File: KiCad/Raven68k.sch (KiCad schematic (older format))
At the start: 19 parts, among them CON1 BARREL_JACK, P1 CONN_01X06, U1 68000D, U2 28C256, U3 SRAM_512Ko, U4 SRAM_512Ko, U5 28C256, U6 XC9572XL-TQ100, Y1 Crystal_GND24

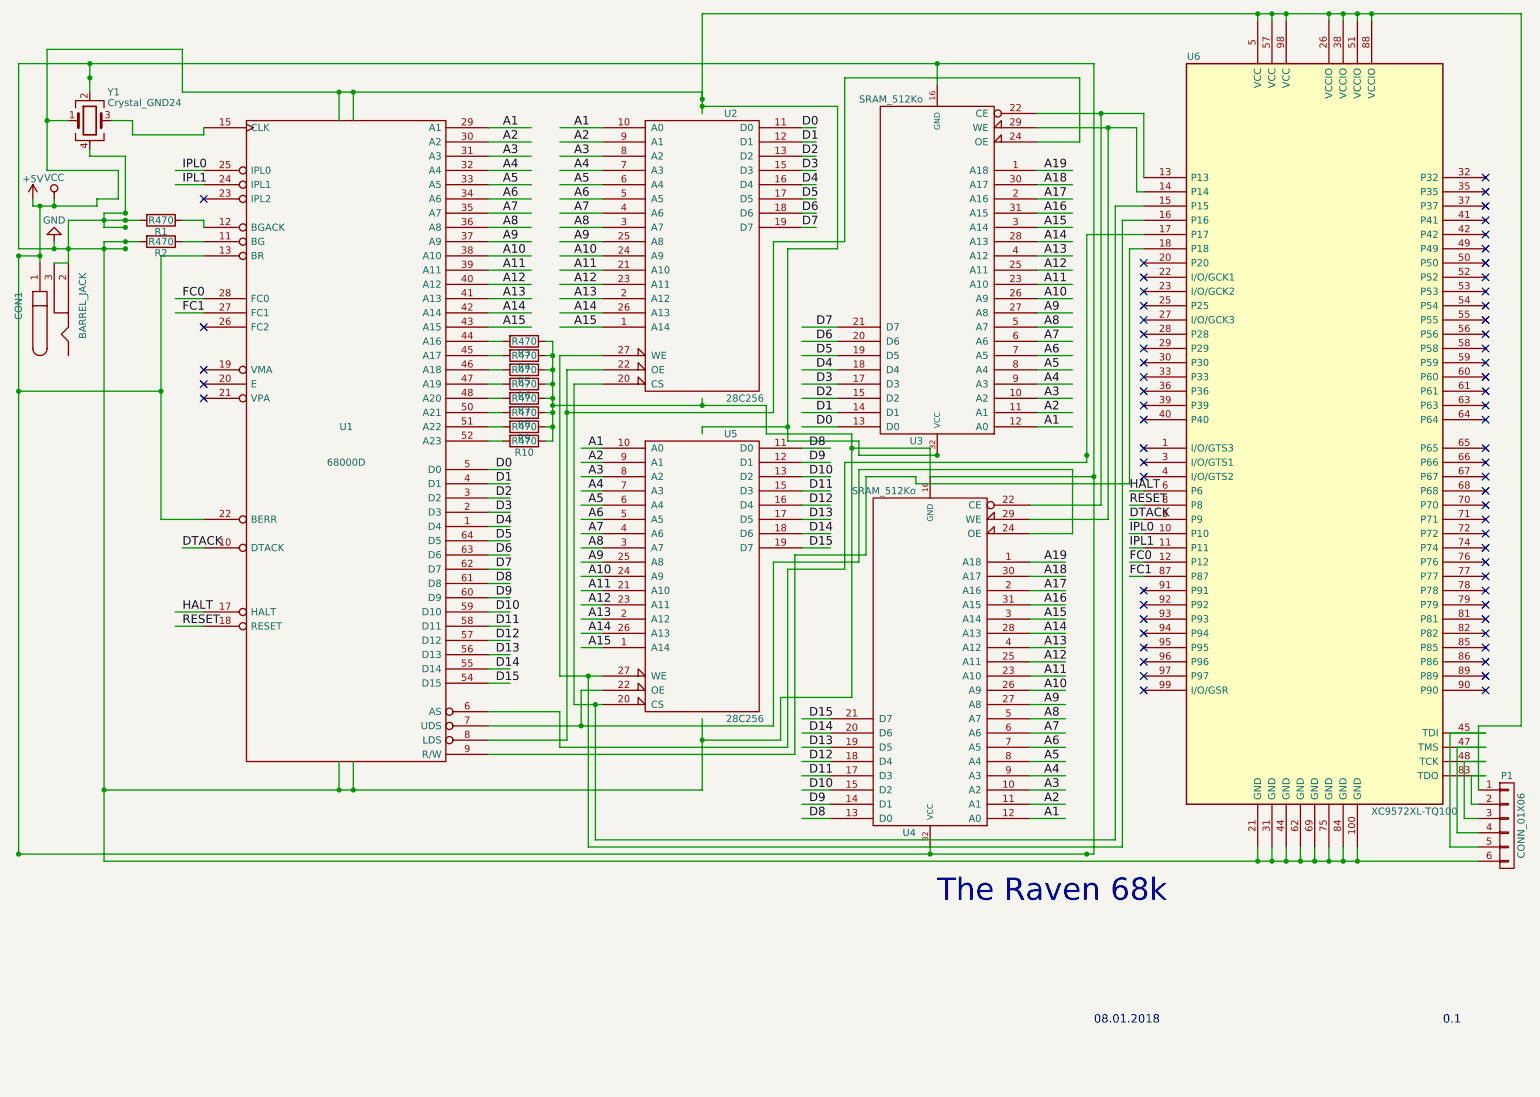
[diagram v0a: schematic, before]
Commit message: Added 68681 DUART.
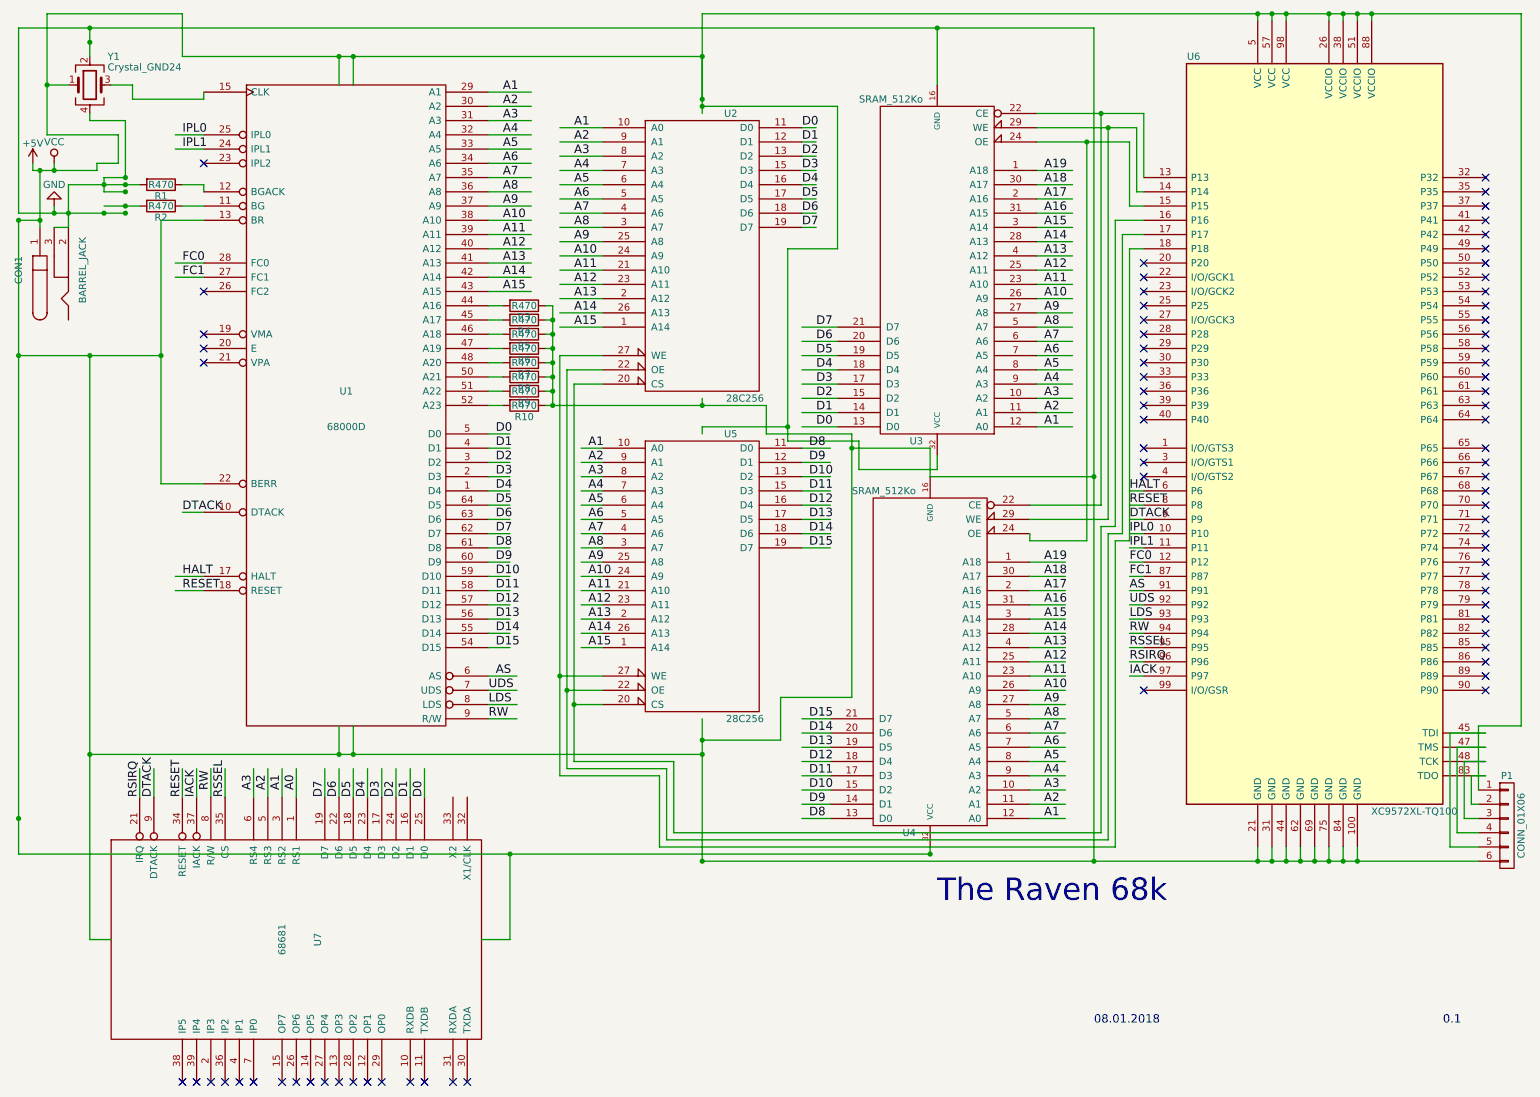
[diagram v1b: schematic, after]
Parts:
- added U7: 68681, symbol 68681
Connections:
- net labels added: A0, AS, IACK, LDS, RSIRQ, RSSEL, RW, UDS
- wire segments 328 -> 345
- no-connect marks 64 -> 75
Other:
- moved on the sheet: CON1, R1, R10, R2, R3, R4, R5, R6, R7, R8, R9, U1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

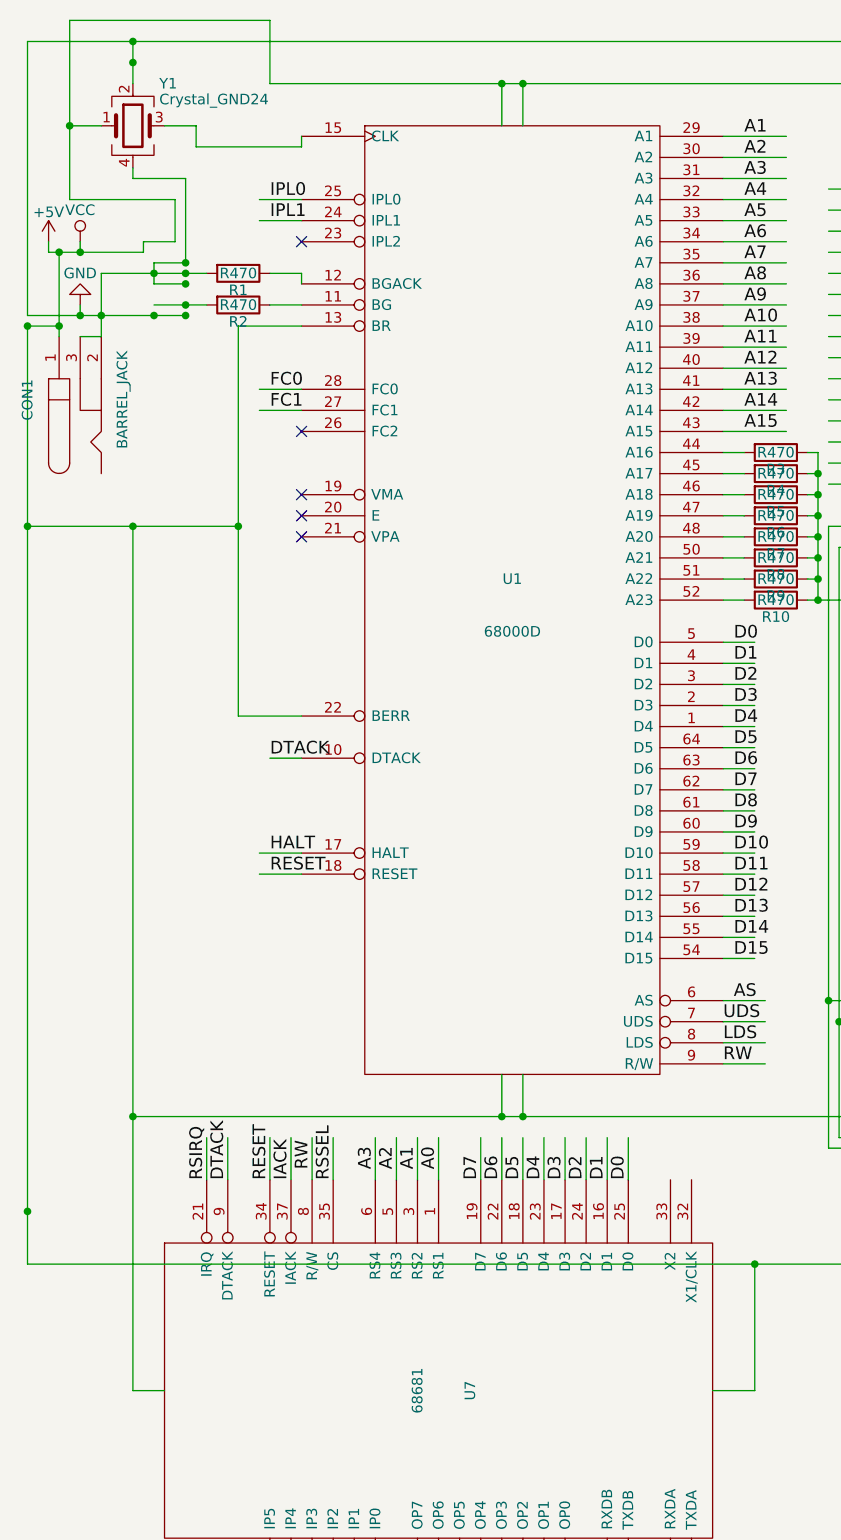
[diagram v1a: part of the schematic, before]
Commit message: Added a few pull-down resistors. Continued schematic re-work started in earlier commit.
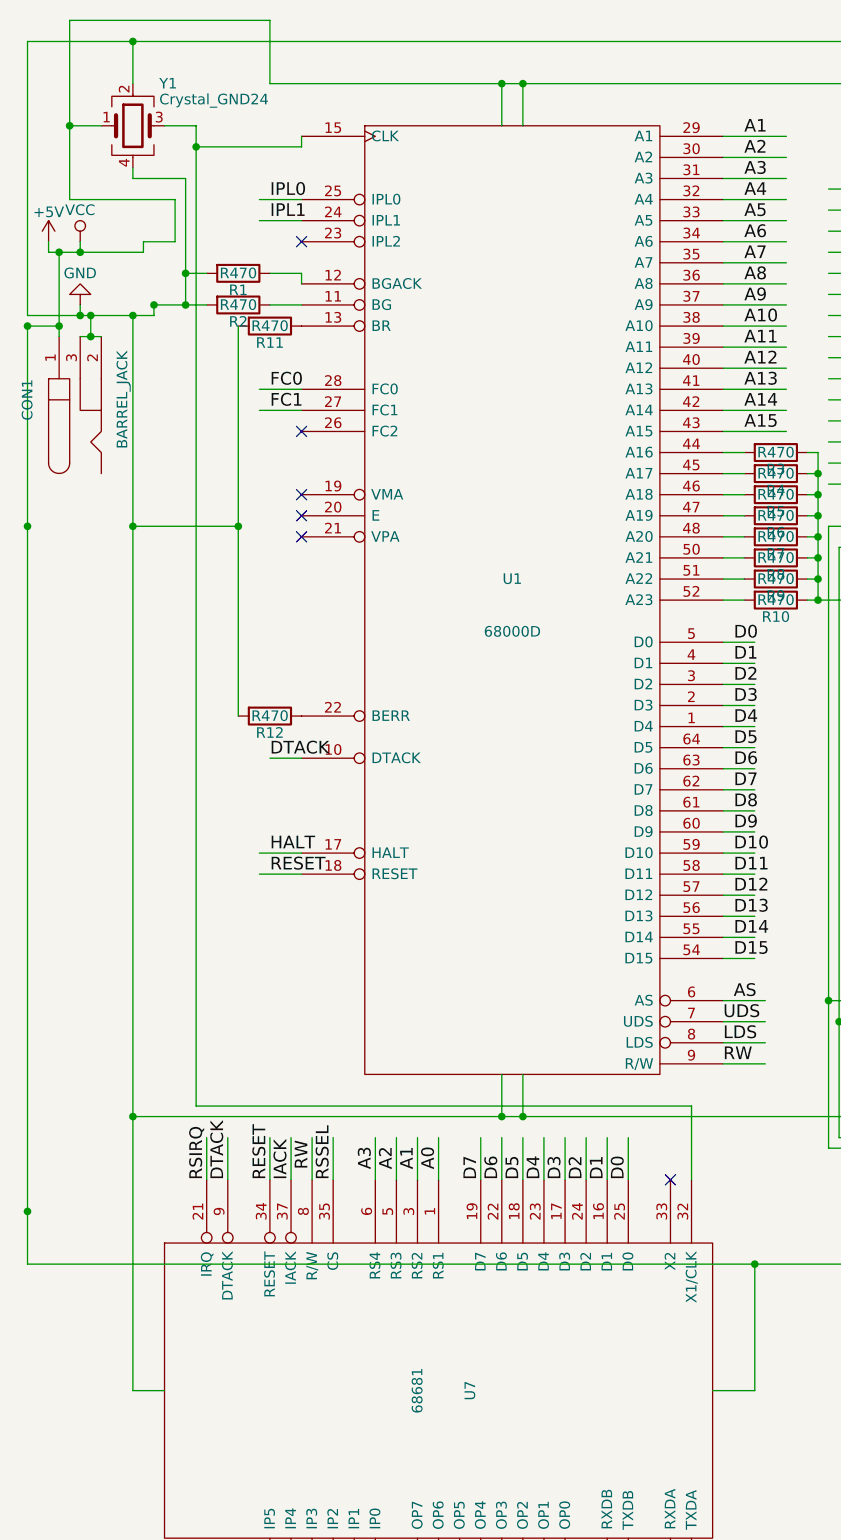
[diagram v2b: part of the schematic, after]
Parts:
- added R11, R12: R470, Resistors_Universal:Resistor_SMD+THTuniversal_1206_RM10_HandSoldering, symbol R
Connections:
- wire segments 345 -> 343
- no-connect marks 75 -> 76
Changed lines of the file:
@@
 	1900 1150 1400 1150
 Wire Wire Line
-	1400 1150 1400 1050
+	1400 1050 1400 5700
 Wire Wire Line
 	1400 1050 1250 1050
@@
 	800  1050 950  1050
 Wire Wire Line
-	1200 1700 1350 1700
-Wire Wire Line
 	1350 1300 1100 1300
 Wire Wire Line
 	1100 1300 1100 1250
-Connection ~ 1350 1700
-Wire Wire Line
-	1350 1950 600  1950
 Wire Wire Line
 	1900 1800 1900 1750
@@
 Wire Wire Line
 	1900 1900 1750 1900
-Wire Wire Line
-	950  1750 1450 1750
 Connection ~ 1350 1750
 Wire Wire Line
@@
 Wire Wire Line
 	1900 4050 1750 4050
-Connection ~ 1200 1950
-Wire Wire Line
-	1200 1800 1350 1800
-Connection ~ 1350 1800
-Connection ~ 1350 1950
 Connection ~ 800  1050
 Wire Wire Line
@@
 Wire Wire Line
 	600  650  8150 650
-Connection ~ 1100 750
-Wire Wire Line
-	1200 1700 1200 1800
-Connection ~ 1200 1750
 Wire Wire Line
 	1300 1600 1150 1600
@@
 Wire Wire Line
 	950  2050 850  2050
-Wire Wire Line
-	950  1750 950  2050
-Connection ~ 950  1950
 Connection ~ 750  1650
 Wire Wire Line
-	1350 1700 1350 1300
+	1350 1300 1350 1900
 Wire Wire Line
 	4700 3600 4550 3600
@@
 Connection ~ 2950 850
 Wire Wire Line
-	1900 2000 1600 2000
-Wire Wire Line
 	1600 2000 1600 3850
-Wire Wire Line
-	1600 3850 1900 3850
-Wire Wire Line
-	1600 2950 600  2950
 Connection ~ 600  2950
 Connection ~ 1600 2950
@@
 	1100 7050 1250 7050
 Wire Wire Line
-	1100 2950 1100 7050
+	1100 1950 1100 7050
 Wire Wire Line
 	1550 6050 1550 5850
@@
 Wire Wire Line
 	5400 6500 10850 6500
+Wire Wire Line
+	1600 2950 1100 2950
+Connection ~ 1100 1950
+Wire Wire Line
+	600  1950 1200 1950
+Connection ~ 1200 1900
+Wire Wire Line
+	1350 1750 1450 1750
+Wire Wire Line
+	1200 1950 1200 1900
+Wire Wire Line
+	900  2050 900  1950
+Connection ~ 900  1950
+Connection ~ 900  2050
+$Comp
+L R R12
+U 1 1 5A58C111
+P 1750 3850
+F 0 "R12" V 1830 3850 50  0000 C CNN
+F 1 "R470" V 1750 3850 50  0000 C CNN
+F 2 "Resistors_Universal:Resistor_SMD+THTuniversal_1206_RM10_HandSoldering" V 1680 3850 50  0001 C CNN
+F 3 "" H 1750 3850 50  0000 C CNN
+	1    1750 3850
+	0    1    1    0
+$EndComp
+$Comp
+L R R11
+U 1 1 5A58C226
+P 1750 2000
+F 0 "R11" V 1830 2000 50  0000 C CNN
+F 1 "R470" V 1750 2000 50  0000 C CNN
+F 2 "Resistors_Universal:Resistor_SMD+THTuniversal_1206_RM10_HandSoldering" V 1680 2000 50  0001 C CNN
+F 3 "" H 1750 2000 50  0000 C CNN
+	1    1750 2000
+	0    1    1    0
+$EndComp
+Wire Wire Line
+	1400 5700 3750 5700
+Wire Wire Line
+	3750 5700 3750 6050
+Connection ~ 1400 1150
+NoConn ~ 3650 6050
 $EndSCHEMATC
